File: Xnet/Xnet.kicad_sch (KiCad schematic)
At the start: 8 parts, among them J401 RJ12, J402 RJ12, U401 MAX485E

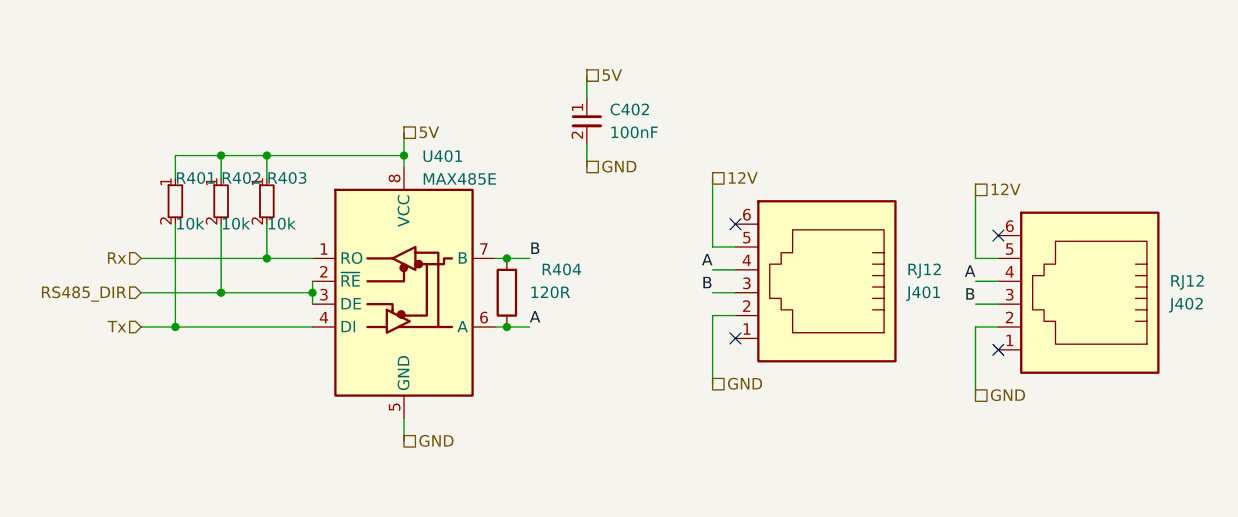
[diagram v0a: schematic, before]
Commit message: removed hierarchial labels for power symbols and replaced them with actual power symbols also updated footprint of the inductor of the 5V buck
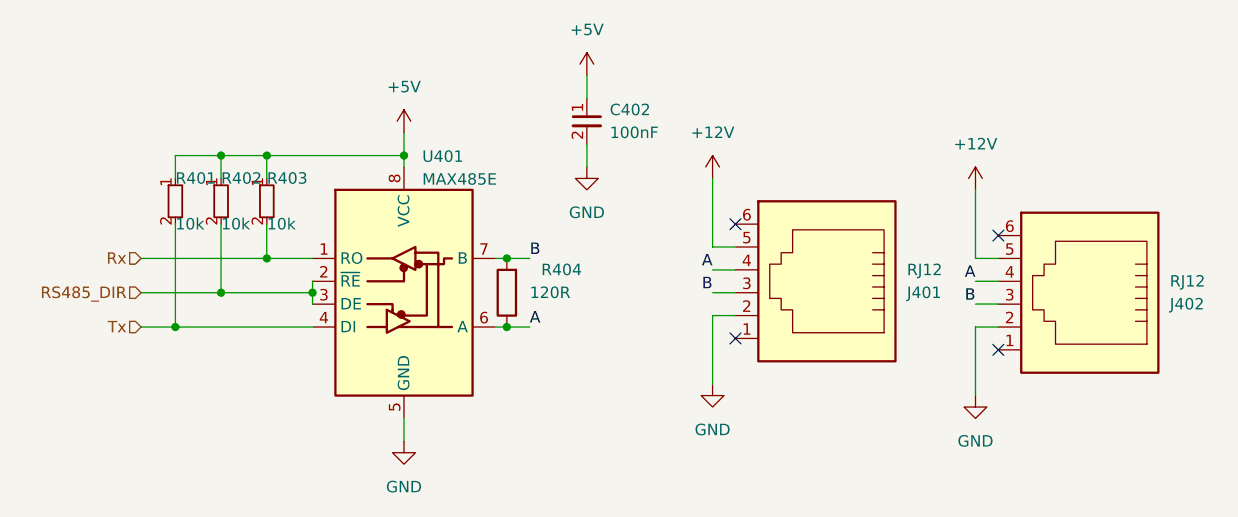
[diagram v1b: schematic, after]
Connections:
- net 12V renamed +12V
- net 5V renamed +5V
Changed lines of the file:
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@@
     (effects (font (size 1.27 1.27)) (justify right))
-  )
-  (hierarchical_label "GND" (shape passive) (at 105.41 97.79 0) (fields_autoplaced)
-    (effects (font (size 1.27 1.27)) (justify left))
-  )
-  (hierarchical_label "GND" (shape passive) (at 134.62 99.06 0) (fields_autoplaced)
-    (effects (font (size 1.27 1.27)) (justify left))
-  )
-  (hierarchical_label "GND" (shape passive) (at 91.44 73.66 0) (fields_autoplaced)
-    (effects (font (size 1.27 1.27)) (justify left))
   )
   (hierarchical_label "Rx" (shape input) (at 41.91 83.82 180) (fields_autoplaced)
     (effects (font (size 1.27 1.27)) (justify right))
   )
-  (hierarchical_label "12V" (shape passive) (at 134.62 76.2 0) (fields_autoplaced)
-    (effects (font (size 1.27 1.27)) (justify left))
-  )
-  (hierarchical_label "GND" (shape passive) (at 71.12 104.14 0) (fields_autoplaced)
-    (effects (font (size 1.27 1.27)) (justify left))
-  )
-  (hierarchical_label "5V" (shape passive) (at 91.44 63.5 0) (fields_autoplaced)
-    (effects (font (size 1.27 1.27)) (justify left))
-  )
   (hierarchical_label "Tx" (shape input) (at 41.91 91.44 180) (fields_autoplaced)
     (effects (font (size 1.27 1.27)) (justify right))
   )
-  (hierarchical_label "12V" (shape passive) (at 105.41 74.93 0) (fields_autoplaced)
-    (effects (font (size 1.27 1.27)) (justify left))
-  )
-  (hierarchical_label "5V" (shape passive) (at 71.12 69.85 0) (fields_autoplaced)
-    (effects (font (size 1.27 1.27)) (justify left))
+  (symbol (lib_id "power:GND") (at 105.41 97.79 0) (unit 1)
+    (in_bom yes) (on_board yes) (dnp no) (fields_autoplaced)
+    (property "Reference" "#PWR0403" (at 105.41 104.14 0)
+      (effects (font (size 1.27 1.27)) hide)
+    )
+    (property "Value" "GND" (at 105.41 102.87 0)
+      (effects (font (size 1.27 1.27)))
+    )
+    (property "Footprint" "" (at 105.41 97.79 0)
+      (effects (font (size 1.27 1.27)) hide)
+    )
+    (property "Datasheet" "" (at 105.41 97.79 0)
+      (effects (font (size 1.27 1.27)) hide)
+    )
+    (pin "1")
+    (instances
+      (project "Xnet"
+        (path "/df188e2b-6a25-44a4-a83d-a1c4efcf9e12"
+          (reference "#PWR0403") (unit 1)
+        )
+      )
+    )
   )
   (symbol (lib_id "Device:R") (at 82.55 87.63 180) (unit 1)
@@
         (path "/df188e2b-6a25-44a4-a83d-a1c4efcf9e12"
           (reference "R403") (unit 1)
+        )
+      )
+    )
+  )
+  (symbol (lib_id "power:+12V") (at 105.41 74.93 0) (unit 1)
+    (in_bom yes) (on_board yes) (dnp no) (fields_autoplaced)
+    (property "Reference" "#PWR0401" (at 105.41 78.74 0)
+      (effects (font (size 1.27 1.27)) hide)
+    )
+    (property "Value" "+12V" (at 105.41 69.85 0)
+      (effects (font (size 1.27 1.27)))
+    )
+    (property "Footprint" "" (at 105.41 74.93 0)
+      (effects (font (size 1.27 1.27)) hide)
+    )
+    (property "Datasheet" "" (at 105.41 74.93 0)
+      (effects (font (size 1.27 1.27)) hide)
+    )
+    (pin "1")
+    (instances
+      (project "Xnet"
+        (path "/df188e2b-6a25-44a4-a83d-a1c4efcf9e12"
+          (reference "#PWR0401") (unit 1)
+        )
+      )
+    )
+  )
+  (symbol (lib_id "power:GND") (at 71.12 104.14 0) (unit 1)
+    (in_bom yes) (on_board yes) (dnp no) (fields_autoplaced)
+    (property "Reference" "#PWR0405" (at 71.12 110.49 0)
+      (effects (font (size 1.27 1.27)) hide)
+    )
+    (property "Value" "GND" (at 71.12 109.22 0)
+      (effects (font (size 1.27 1.27)))
+    )
+    (property "Footprint" "" (at 71.12 104.14 0)
+      (effects (font (size 1.27 1.27)) hide)
+    )
+    (property "Datasheet" "" (at 71.12 104.14 0)
+      (effects (font (size 1.27 1.27)) hide)
+    )
+    (pin "1")
+    (instances
+      (project "Xnet"
+        (path "/df188e2b-6a25-44a4-a83d-a1c4efcf9e12"
+          (reference "#PWR0405") (unit 1)
+        )
+      )
+    )
+  )
+  (symbol (lib_id "power:GND") (at 134.62 99.06 0) (unit 1)
+    (in_bom yes) (on_board yes) (dnp no) (fields_autoplaced)
+    (property "Reference" "#PWR0404" (at 134.62 105.41 0)
+      (effects (font (size 1.27 1.27)) hide)
+    )
+    (property "Value" "GND" (at 134.62 104.14 0)
+      (effects (font (size 1.27 1.27)))
+    )
+    (property "Footprint" "" (at 134.62 99.06 0)
+      (effects (font (size 1.27 1.27)) hide)
+    )
+    (property "Datasheet" "" (at 134.62 99.06 0)
+      (effects (font (size 1.27 1.27)) hide)
+    )
+    (pin "1")
+    (instances
+      (project "Xnet"
+        (path "/df188e2b-6a25-44a4-a83d-a1c4efcf9e12"
+          (reference "#PWR0404") (unit 1)
         )
       )
@@
         )
       )
+    )
+  )
+  (symbol (lib_id "power:+5V") (at 91.44 63.5 0) (unit 1)
+    (in_bom yes) (on_board yes) (dnp no) (fields_autoplaced)
+    (property "Reference" "#PWR0408" (at 91.44 67.31 0)
+      (effects (font (size 1.27 1.27)) hide)
+    )
+    (property "Value" "+5V" (at 91.44 58.42 0)
+      (effects (font (size 1.27 1.27)))
+    )
+    (property "Footprint" "" (at 91.44 63.5 0)
+      (effects (font (size 1.27 1.27)) hide)
+    )
+    (property "Datasheet" "" (at 91.44 63.5 0)
+      (effects (font (size 1.27 1.27)) hide)
+    )
+    (pin "1")
+    (instances
+      (project "Xnet"
+        (path "/df188e2b-6a25-44a4-a83d-a1c4efcf9e12"
+          (reference "#PWR0408") (unit 1)
+        )
+      )
+    )
+  )
+  (symbol (lib_id "power:GND") (at 91.44 73.66 0) (unit 1)
+    (in_bom yes) (on_board yes) (dnp no) (fields_autoplaced)
+    (property "Reference" "#PWR0407" (at 91.44 80.01 0)
+      (effects (font (size 1.27 1.27)) hide)
+    )
+    (property "Value" "GND" (at 91.44 78.74 0)
+      (effects (font (size 1.27 1.27)))
+    )
+    (property "Footprint" "" (at 91.44 73.66 0)
+      (effects (font (size 1.27 1.27)) hide)
+    )
+    (property "Datasheet" "" (at 91.44 73.66 0)
+      (effects (font (size 1.27 1.27)) hide)
+    )
+    (pin "1")
+    (instances
+      (project "Xnet"
+        (path "/df188e2b-6a25-44a4-a83d-a1c4efcf9e12"
+          (reference "#PWR0407") (unit 1)
+        )
+      )
+    )
+  )
+  (symbol (lib_id "power:+12V") (at 134.62 76.2 0) (unit 1)
+    (in_bom yes) (on_board yes) (dnp no) (fields_autoplaced)
+    (property "Reference" "#PWR0402" (at 134.62 80.01 0)
+      (effects (font (size 1.27 1.27)) hide)
+    )
+    (property "Value" "+12V" (at 134.62 71.12 0)
+      (effects (font (size 1.27 1.27)))
+    )
+    (property "Footprint" "" (at 134.62 76.2 0)
+      (effects (font (size 1.27 1.27)) hide)
+    )
+    (property "Datasheet" "" (at 134.62 76.2 0)
+      (effects (font (size 1.27 1.27)) hide)
+    )
+    (pin "1")
+    (instances
+      (project "Xnet"
+        (path "/df188e2b-6a25-44a4-a83d-a1c4efcf9e12"
+          (reference "#PWR0402") (unit 1)
+        )
+      )
+    )
+  )
+  (symbol (lib_id "power:+5V") (at 71.12 69.85 0) (unit 1)
+    (in_bom yes) (on_board yes) (dnp no) (fields_autoplaced)
+    (property "Reference" "#PWR0406" (at 71.12 73.66 0)
+      (effects (font (size 1.27 1.27)) hide)
+    )
+    (property "Value" "+5V" (at 71.12 64.77 0)
+      (effects (font (size 1.27 1.27)))
+    )
+    (property "Footprint" "" (at 71.12 69.85 0)
+      (effects (font (size 1.27 1.27)) hide)
+    )
+    (property "Datasheet" "" (at 71.12 69.85 0)
+      (effects (font (size 1.27 1.27)) hide)
+    )
+    (pin "1")
+    (instances
+      (project "Xnet"
+        (path "/df188e2b-6a25-44a4-a83d-a1c4efcf9e12"
+          (reference "#PWR0406") (unit 1)
+        )
+      )
